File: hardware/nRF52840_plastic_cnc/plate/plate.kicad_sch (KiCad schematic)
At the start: 86 parts

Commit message: M  hardware/nRF52840_plastic_cnc/border.py M  hardware/nRF52840_plastic_cnc/pcb/pcb-Edge_Cuts.dxf M  hardware/nRF52840_plastic_cnc/pcb/pcb.kicad_pcb M  hardware/nRF52840_plastic_cnc/pcb/pcb.kicad_prl M  hardware/nRF52840_plastic_cnc/pcb/pcb.kicad_sch M  hardware/nRF52840_plastic_cnc/placefp.py M  hardware/nRF52840_plastic_cnc/plate/plate.kicad_pcb M  hardware/nRF52840_plastic_cnc/plate/plate.kicad_sch
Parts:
- S46: footprint tmr-lib:Switch_Cutout -> tmr-lib:Switch_Cutout_1.75u
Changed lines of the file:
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@@
 			)
 		)
-		(property "Footprint" "tmr-lib:Switch_Cutout"
+		(property "Footprint" "tmr-lib:Switch_Cutout_1.75u"
 			(at 68.58 78.74 0)
 			(effects

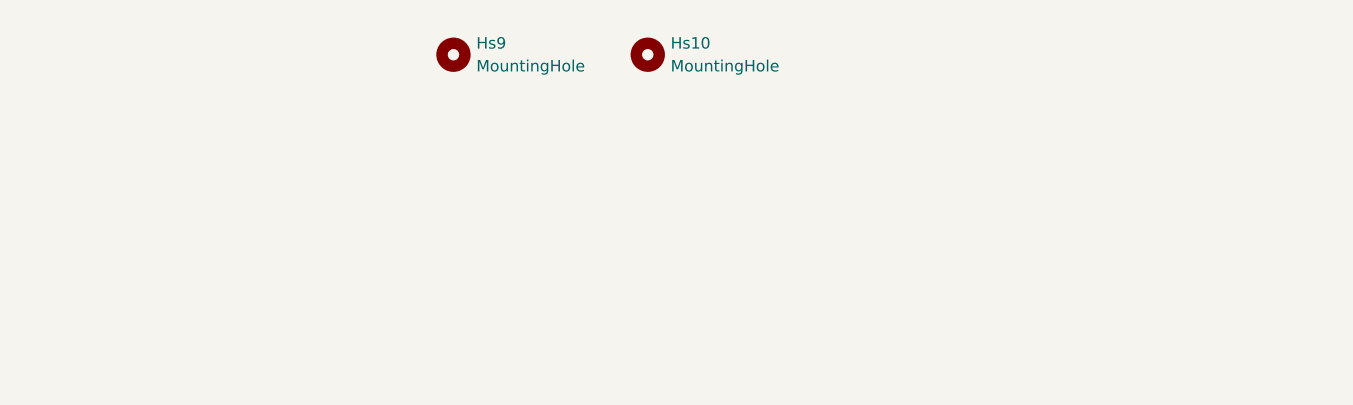
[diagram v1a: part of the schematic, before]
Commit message: M  hardware/nRF52840_plastic_cnc/border.py A  hardware/nRF52840_plastic_cnc/pcb/pcb-User_1.dxf A  hardware/nRF52840_plastic_cnc/pcb/pcb-User_2.dxf A  hardware/nRF52840_plastic_cnc/pcb/pcb-User_3.dxf M  hardware/nRF52840_plastic_cnc/pcb/pcb.kicad_pcb M  hardware/nRF52840_plastic_cnc/pcb/pcb.kicad_prl M  hardware/nRF52840_plastic_cnc/placefp.py M  hardware/nRF52840_plastic_cnc/plate/plate.kicad_pcb M  hardware/nRF52840_plastic_cnc/plate/plate.kicad_sch M  hardware/nRF52840_plastic_cnc/tmr-footprints/Gateron_Switch_Lowpro.kicad_mod A  hardware/nRF52840_plastic_cnc/tmr-footprints/M2_HeatSinkNut_Flanged.kicad_mod
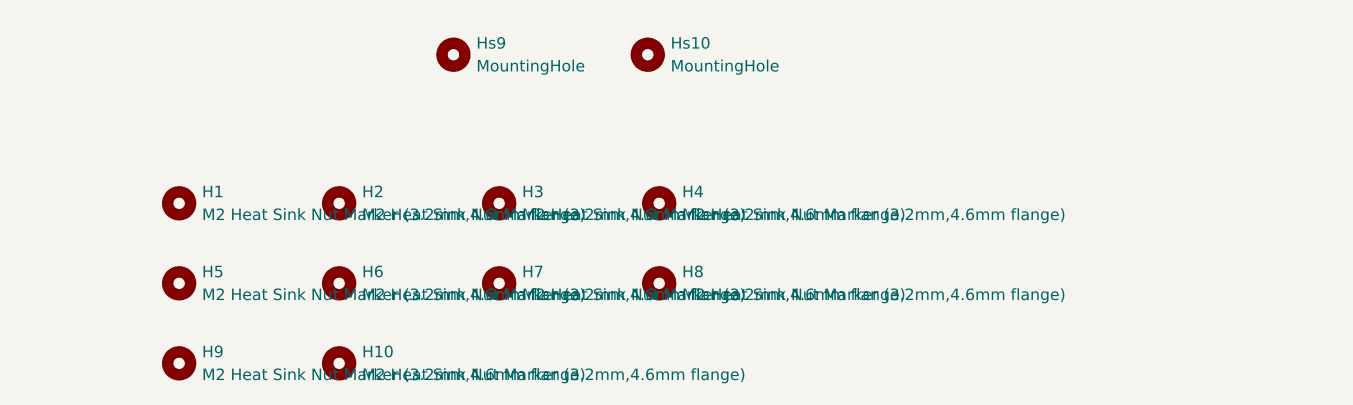
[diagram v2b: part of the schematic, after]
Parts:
- added H1, H10, H2, H3, H4, H5, H6, H7, H8, H9: M2 Heat Sink Nut Marker (3.2mm,4.6mm flange), tmr-lib:M2_HeatSinkNut_Flanged, symbol Mechanical:MountingHole
